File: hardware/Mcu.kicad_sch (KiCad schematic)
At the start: 14 parts, among them U11 STM32H573RIVx, Y1 X322516MLB4SI

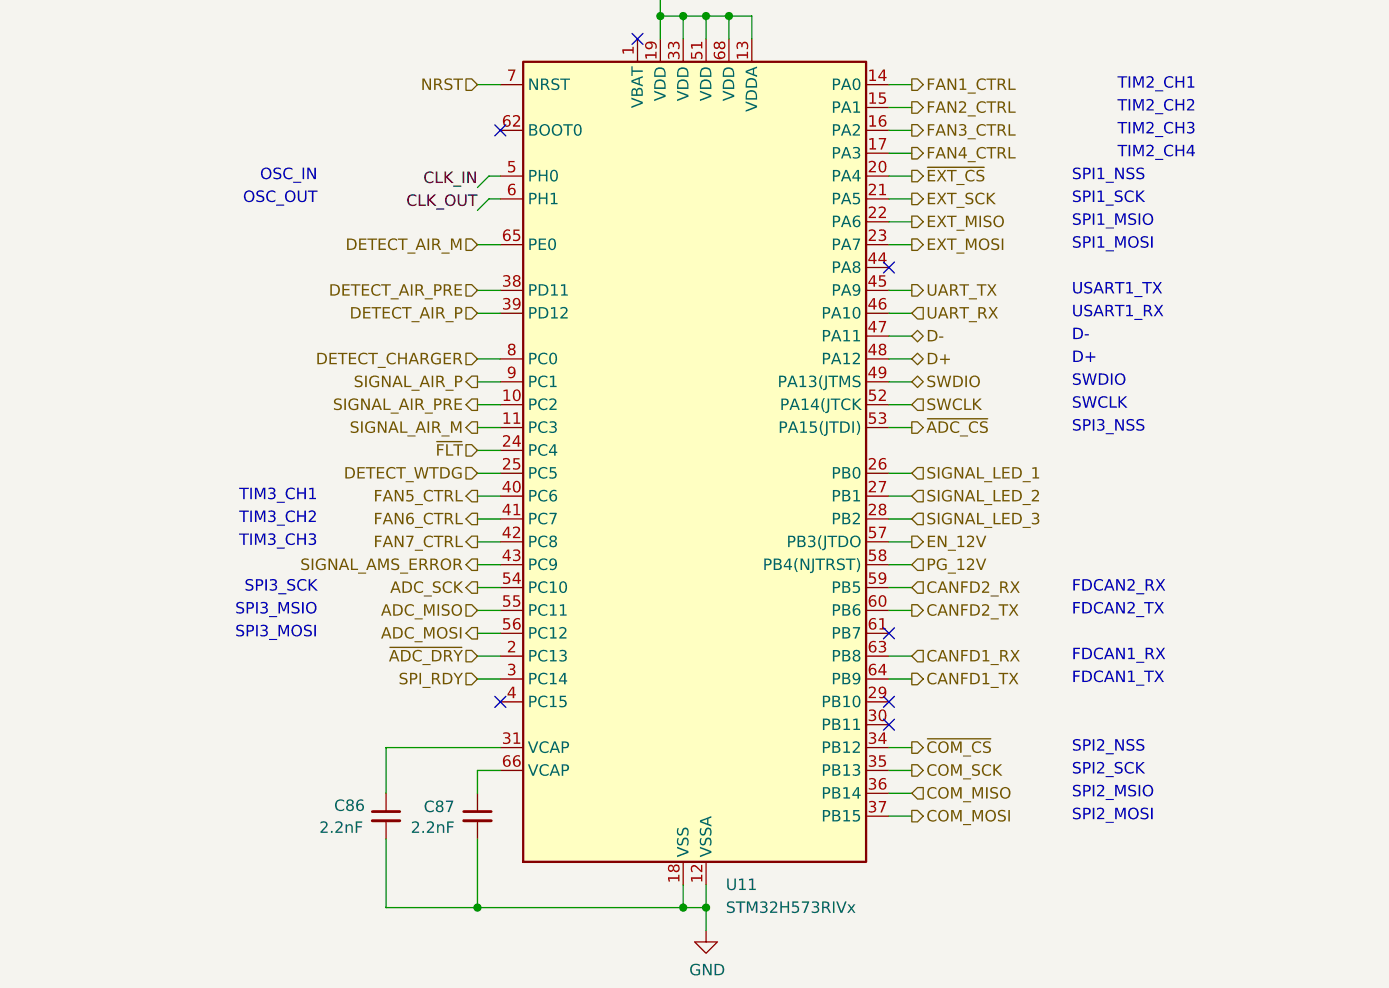
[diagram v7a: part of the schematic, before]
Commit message: changing mcu done + new routing
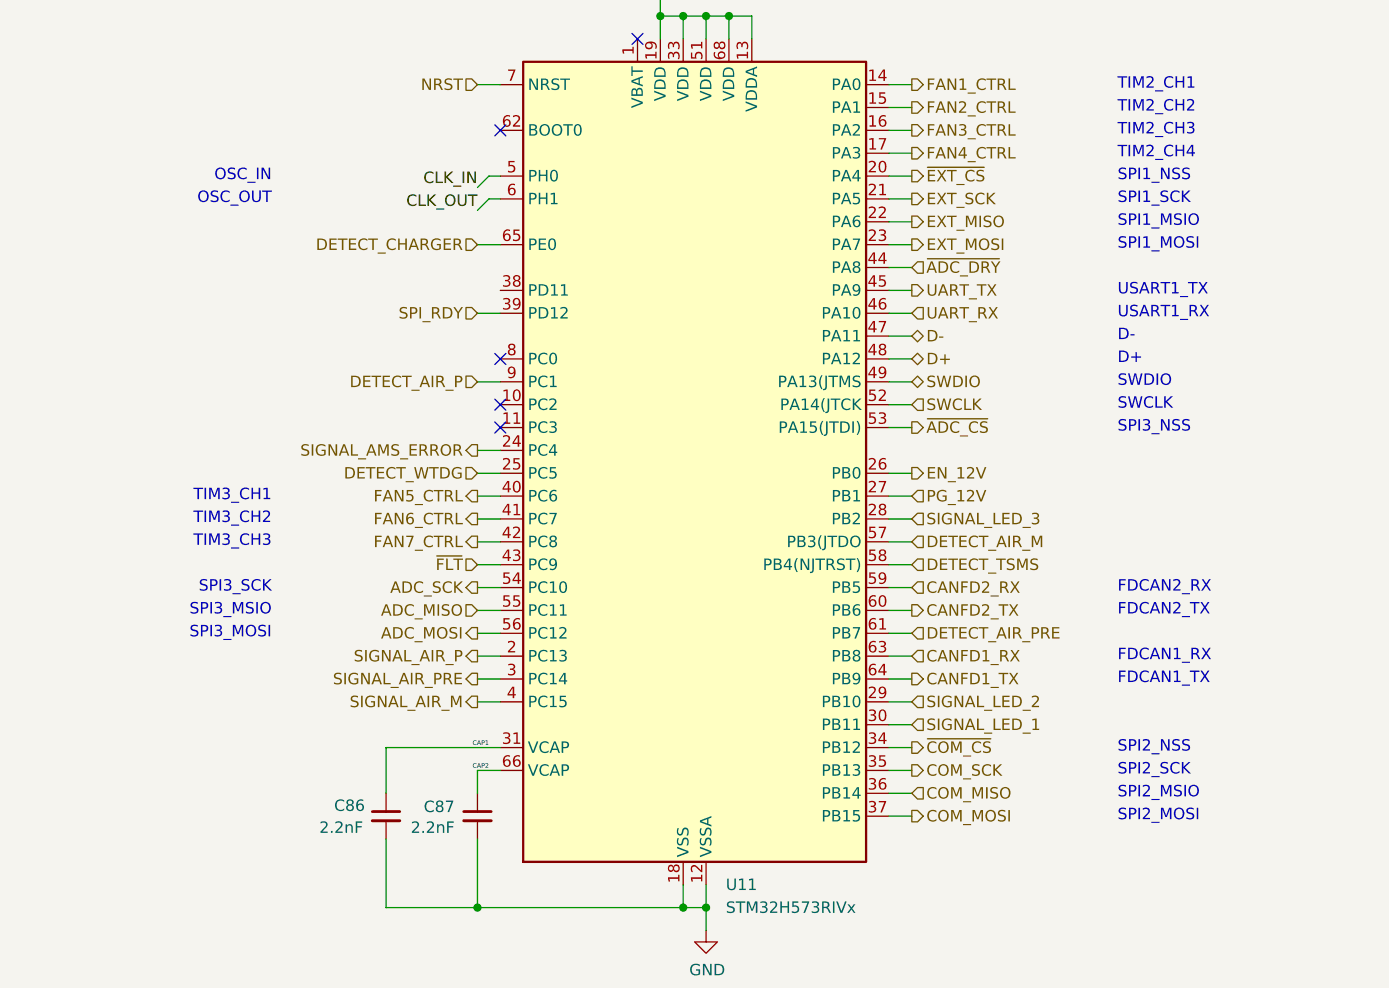
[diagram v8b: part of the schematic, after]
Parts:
- C86, C87: footprint Capacitor_SMD:C_0402_1005Metric -> Capacitor_SMD:C_0603_1608Metric
- U11: footprint Package_DFN_QFN:QFN-68-1EP_8x8mm_P0.4mm_EP5.2x5.2mm -> Package_DFN_QFN:QFN-68-1EP_8x8mm_P0.4mm_EP6.4x6.4mm
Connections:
- net DETECT_AIR_M: now also U11.57 (PB3(JTDO); no longer U11.65 (PE0)
- net DETECT_AIR_P: now also U11.9 (PC1); no longer U11.39 (PD12)
- net DETECT_AIR_PRE: now also U11.61 (PB7); no longer U11.38 (PD11)
- net DETECT_CHARGER: now also U11.65 (PE0); no longer U11.8 (PC0)
- net EN_12V: now also U11.26 (PB0); no longer U11.57 (PB3(JTDO)
- net PG_12V: now also U11.27 (PB1); no longer U11.58 (PB4(NJTRST))
- net SIGNAL_AIR_M: now also U11.4 (PC15); no longer U11.11 (PC3)
- net SIGNAL_AIR_P: now also U11.2 (PC13); no longer U11.9 (PC1)
- net SIGNAL_AIR_PRE: now also U11.3 (PC14); no longer U11.10 (PC2)
- net SIGNAL_AMS_ERROR: now also U11.24 (PC4); no longer U11.43 (PC9)
- net SIGNAL_LED_1: now also U11.30 (PB11); no longer U11.26 (PB0)
- net SIGNAL_LED_2: now also U11.29 (PB10); no longer U11.27 (PB1)
- net SPI_RDY: now also U11.39 (PD12); no longer U11.3 (PC14)
- net ~{ADC_DRY}: now also U11.44 (PA8); no longer U11.2 (PC13)
- net ~{FLT}: now also U11.43 (PC9); no longer U11.24 (PC4)
- net CAP2: now reaches C87.1, U11.66 (VCAP)
- net CAP1: now reaches C86.1, U11.31 (VCAP)
- new net DETECT_TSMS: U11.58 (PB4(NJTRST))
- no-connect marks 7 -> 5
